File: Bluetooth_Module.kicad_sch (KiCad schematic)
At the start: 4 parts

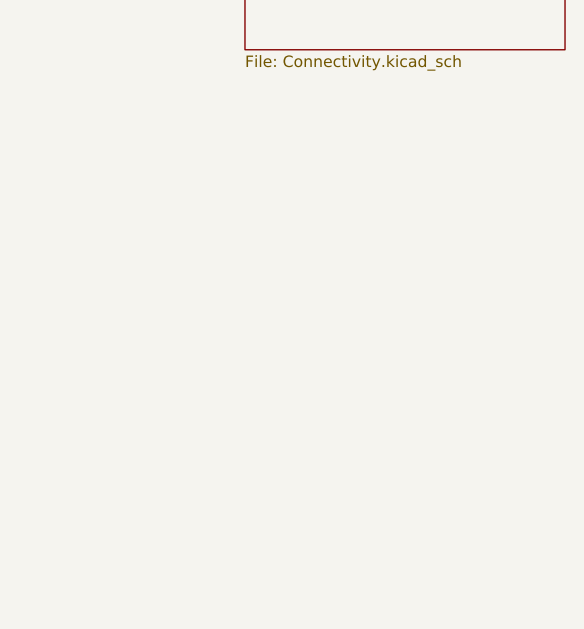
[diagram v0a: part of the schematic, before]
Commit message: Lesson 2 - transistor circuits added
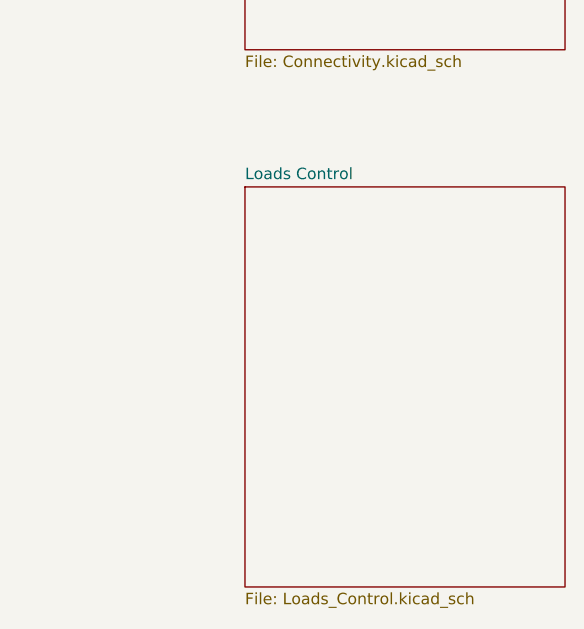
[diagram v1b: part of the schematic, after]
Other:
- added sheet Loads Control (Loads_Control.kicad_sch)
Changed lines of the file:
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@@
+		)
+	)
+	(sheet
+		(at 107.95 100.33)
+		(size 35.56 44.45)
+		(exclude_from_sim no)
+		(in_bom yes)
+		(on_board yes)
+		(dnp no)
+		(fields_autoplaced yes)
+		(stroke
+			(width 0.1524)
+			(type solid)
+		)
+		(fill
+			(color 0 0 0 0.0000)
+		)
+		(property "Sheetname" "Loads Control"
+			(at 107.95 99.6184 0)
+			(effects
+				(font
+					(size 1.27 1.27)
+				)
+				(justify left bottom)
+			)
+		)
+		(property "Sheetfile" "Loads_Control.kicad_sch"
+			(at 107.95 145.3646 0)
+			(effects
+				(font
+					(size 1.27 1.27)
+				)
+				(justify left top)
+			)
+		)
+		(instances
+			(project "Bluetooth_Module"
+				(path "/a0279ad6-d799-42fb-ac0d-b52a8d0ab216"
+					(page "3")
+				)
+			)
 		)
 	)

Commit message: Lesson 4 - Power Supply
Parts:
- removed H2: MountingHole, MountingHole:MountingHole_3.5mm, symbol Mechanical:MountingHole
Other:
- added sheet Power Supply (power_supply.kicad_sch)
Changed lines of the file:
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@@
-	(symbol
-		(lib_id "Mechanical:MountingHole")
-		(at 38.1 16.51 0)
-		(unit 1)
-		(exclude_from_sim no)
-		(in_bom no)
-		(on_board yes)
-		(dnp no)
-		(fields_autoplaced yes)
-		(property "Reference" "H2"
-			(at 40.64 15.2399 0)
-			(effects
-				(font
-					(size 1.27 1.27)
-				)
-				(justify left)
-			)
-		)
-		(property "Value" "MountingHole"
-			(at 40.64 17.7799 0)
-			(effects
-				(font
-					(size 1.27 1.27)
-				)
-				(justify left)
-			)
-		)
-		(property "Footprint" "MountingHole:MountingHole_3.5mm"
-			(at 38.1 16.51 0)
-			(effects
-				(font
-					(size 1.27 1.27)
-				)
-				(hide yes)
-			)
-		)
-		(property "Datasheet" "~"
-			(at 38.1 16.51 0)
-			(effects
-				(font
-					(size 1.27 1.27)
-				)
-				(hide yes)
-			)
-		)
-		(property "Description" "Mounting Hole without connection"
-			(at 38.1 16.51 0)
-			(effects
-				(font
-					(size 1.27 1.27)
-				)
-				(hide yes)
-			)
-		)
-		(instances
-			(project "Bluetooth_Module"
-				(path "/a0279ad6-d799-42fb-ac0d-b52a8d0ab216"
-					(reference "H2")
-					(unit 1)
-				)
-			)
-		)
-	)
 	(symbol
 		(lib_id "Mechanical:MountingHole")
@@
 				)
 			)
+		)
+	)
+	(sheet
+		(at 157.48 43.18)
+		(size 35.56 40.64)
+		(exclude_from_sim no)
+		(in_bom yes)
+		(on_board yes)
+		(dnp no)
+		(fields_autoplaced yes)
+		(stroke
+			(width 0.1524)
+			(type solid)
+		)
+		(fill
+			(color 0 0 0 0.0000)
+		)
+		(property "Sheetname" "Power Supply"
+			(at 157.48 42.4684 0)
+			(effects
+				(font
+					(size 1.27 1.27)
+				)
+				(justify left bottom)
+			)
+		)
+		(property "Sheetfile" "power_supply.kicad_sch"
+			(at 157.48 84.4046 0)
+			(effects
+				(font
+					(size 1.27 1.27)
+				)
+				(justify left top)
+			)
+		)
+		(instances
+			(project "Bluetooth_Module"
+				(path "/a0279ad6-d799-42fb-ac0d-b52a8d0ab216"
+					(page "4")
+				)
+			)
